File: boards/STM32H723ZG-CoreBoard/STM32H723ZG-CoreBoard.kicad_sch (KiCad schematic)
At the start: 44 parts, among them J1 USB-C, J2 PORT_L, J3 PORT_B, J4 PORT_R, J5 PORT_T, J6 SWD, SW1 RESET, SW2 BOOT0, U1 STM32H723ZGT6, U2 AP2112K-3.3, Y1 25MHz, Y2 32.768kHz

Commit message: Довести H723 до KiCad 10: разъём прошивки, STDC14, переразметка верхнего кольца
Плата H723 пересобрана в формате KiCad 10 и подтянута к раскладке G474.

Плата:
- разъём прошивки J6 - 1x10 с распиновкой WeAct, развёрнут 5V к востоку,
  SWO садится на PB3 прямой дорожкой;
- добавлен J7 - STDC14 (2x7, 1.27 мм), штатный разъём ST-LINK V3. Стоит
  вертикально сигнальным рядом к J6: строки веера идут по строкам падов и
  между собой не пересекаются, а расходятся по слоям;
- USB-C стоит на плате целиком, D+/D- заведены на PA11/PA12;
- кнопки RST и BOOT0 собраны в колонку у левого края, R4 - вплотную к SW2;
- светодиод и резистор развёрнуты под 45 градусов в углу между J2 и J3;
- подписаны все 144 контакта гребёнок и номиналы всех компонентов.

Генератор:
- gen/kicadenv.py - поиск библиотек KiCad на любой ОС и различия API 7/10;
- gen/export.py - гербера, сверловка, pos.csv, PDF и архив через kicad-cli;
- сборка платы больше не зависит от системных библиотек: футпринты уходят в
  auto_probe.pretty рядом с платой;
- kigen.py: разбор многострочной формы pin_names/pin_numbers KiCad 10 -
  из-за неё поверх номеров контактов печатались имена;
- crtyd.py считает пересечение реальных полигонов, а не описанных
  прямоугольников; drc.py не считает нарушением зазор ровно по правилу.

Проверки H723: DRC KiCad 0 нарушений, 0 несоединённых, 0 расхождений со
схемой; собственный контроль зазоров 0, courtyard 0, шелкография 0.
Файлы платы G474 не тронуты, правки в build_g474.py - только переносимость.

Co-Authored-By: Claude Opus 5 <noreply@anthropic.com>
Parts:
- removed J6: SWD, Connector_PinHeader_2.54mm:PinHeader_1x04_P2.54mm_Vertical, symbol Connector_Generic:Conn_01x04
- added J6: DEBUG, auto_probe:PinHeader_1x10_P2.54mm_Vertical, symbol Connector_Generic:Conn_01x10
- added J7: STDC14, auto_probe:PinHeader_2x07_P1.27mm_Vertical, symbol Connector_Generic:Conn_02x07_Odd_Even
- C1, C10, C11, C2, C3, C4, C5, C6, C60, C61, C62, C63, C7, C70, C74, C77, C8, C9: footprint :C_0402_1005Metric -> auto_probe:C_0402_1005Metric
- C50, C51, C75, C76: footprint :C_0805_2012Metric -> auto_probe:C_0805_2012Metric
- C52, C71, C72, C73: footprint :C_0603_1608Metric -> auto_probe:C_0603_1608Metric
- D1: footprint LED_SMD:LED_0805_2012Metric -> auto_probe:LED_0805_2012Metric
- J1: footprint Connector_USB:USB_C_Receptacle_HRO_TYPE-C-31-M-12 -> auto_probe:USB_C_Receptacle_HRO_TYPE-C-31-M-12
- J2, J3, J4, J5: footprint Connector_PinHeader_2.54mm:PinHeader_2x18_P2.54mm_Vertical -> auto_probe:PinHeader_2x18_P2.54mm_Vertical
- R1, R2, R3, R4, R5: footprint Resistor_SMD:R_0402_1005Metric -> auto_probe:R_0402_1005Metric
- SW1, SW2: footprint Button_Switch_SMD:SW_SPST_SKQG_WithoutStem -> auto_probe:SW_SPST_SKQG_WithoutStem
- U1: footprint Package_QFP:LQFP-144_20x20mm_P0.5mm -> auto_probe:LQFP-144_20x20mm_P0.5mm
- U2: footprint Package_TO_SOT_SMD:SOT-23-5 -> auto_probe:SOT-23-5
- Y1: footprint Crystal:Crystal_SMD_5032-2Pin_5.0x3.2mm -> auto_probe:Crystal_SMD_5032-2Pin_5.0x3.2mm
- Y2: footprint Crystal:Crystal_SMD_MicroCrystal_CC7V-T1A-2Pin_3.2x1.5mm -> auto_probe:Crystal_SMD_MicroCrystal_CC7V-T1A-2Pin_3.2x1.5mm
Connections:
- net +3V3: now also J6.10 (Pin_10), J7.3 (Pin_3)
- net GND: now also J1.SH (SHIELD), J6.2 (Pin_2), J6.7 (Pin_7), J7.11 (Pin_11), J7.5 (Pin_5), J7.7 (Pin_7); no longer J1.S1 (SHIELD)
- net NRST: now also J6.5 (Pin_5), J7.12 (Pin_12)
- net PB3: now also J6.6 (Pin_6), J7.8 (Pin_8)
- net PC10: now also J6.3 (Pin_3)
- net PC11: now also J6.4 (Pin_4)
- net SWCLK: now also J6.8 (Pin_8), J7.6 (Pin_6)
- net SWDIO: now also J6.9 (Pin_9), J7.4 (Pin_4)
- net VBUS: now also J6.1 (Pin_1)
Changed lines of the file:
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@@
 (kicad_sch (version 20230121) (generator kigen)
-  (paper "A2")
+  (paper "A1")
   (title_block
     (title "STM32H723ZGT6 core board (LQFP144) - 84x84 mm, 4 layers")

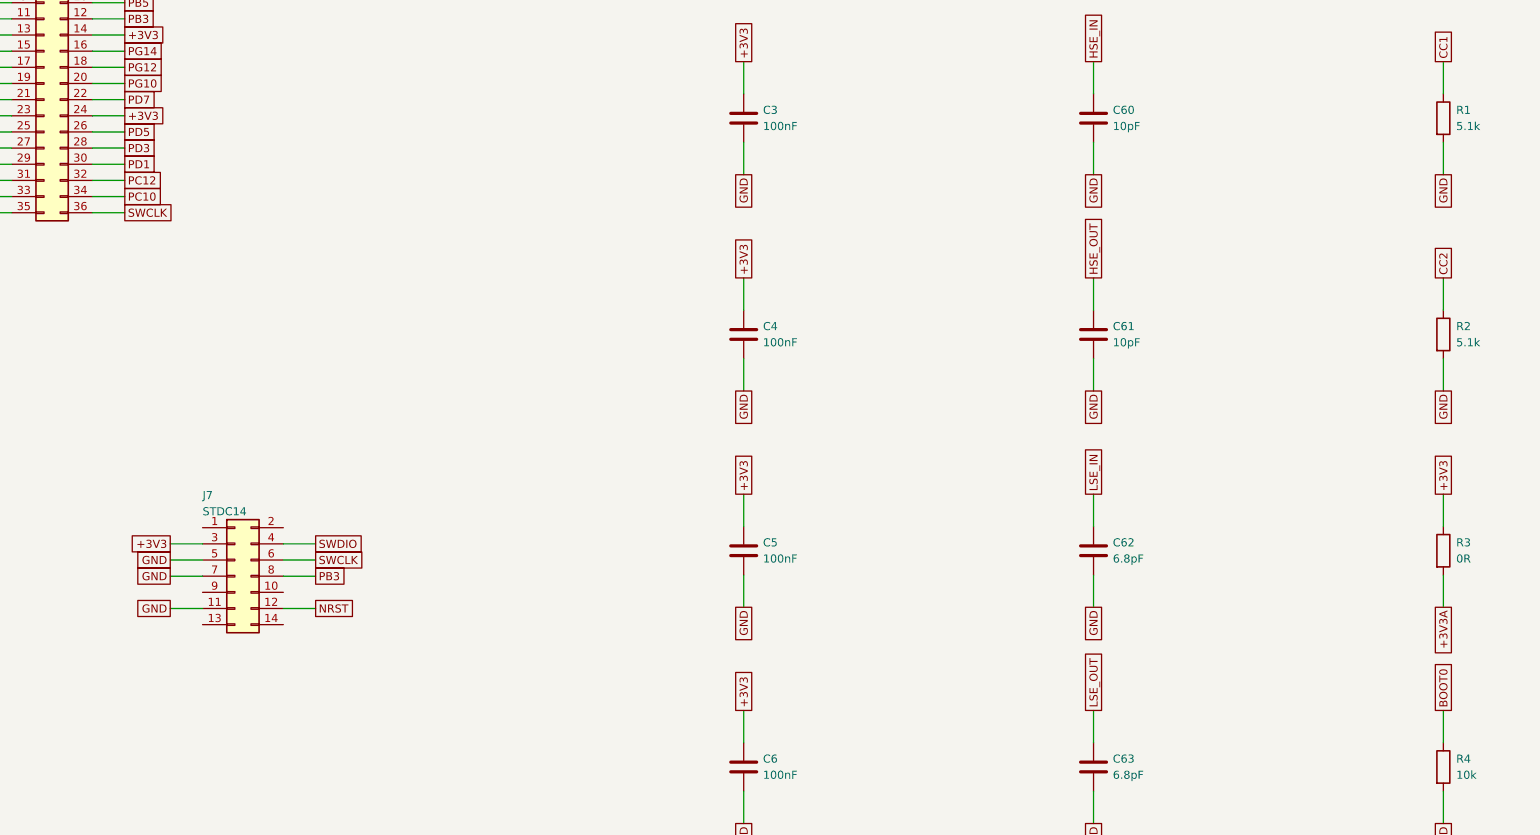
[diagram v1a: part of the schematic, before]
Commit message: H723: убрать STDC14, переразметить верхнее кольцо и шелкографию под нормы печати
Разъём прошивки и его окружение:
- STDC14 (J7) снят с платы, из схемы и из библиотеки проекта: вертикально он
  занимал 7.6 мм по высоте и не давал поднять J6;
- J6 поднят к верхнему краю (Y0+5.2), обозначение закреплено в торце справа;
- полосы SWO/CLK/DIO отведены от контура: было 0.67 мм до фрезы, стало 1.67;
- BOOT0 к гребёнке обходит J6 западнее, отвод +3V3 от контакта 10 смотрит вверх.

Шелкография приведена к нормам JLCPCB (0.8 мм при линии 0.15):
- подписи контактов были 0.6/0.1, номиналы на обратной стороне 0.5 - мельче
  минимума, при печати такие символы плывут;
- строки подписей отодвинуты от гребёнок, внешние выставлены по центру кольца:
  крупный шрифт задевал контур разъёма и свешивался за край платы;
- в кольце 3.7 мм, пятизначное имя туда не входит - для нескольких цепей на
  шелке короткая форма (3V3A, PC2C, USBDP); в схеме и PINOUT.csv имена полные;
- у деталей печатается только обозначение, номиналы собраны в таблицу
  "обозначение - номинал" на 35 строк в двух свободных площадках у J4;
- обозначение ставится строго над своей деталью горизонтально: раньше список
  занятых мест включал их же штатные позиции, подпись конфликтовала сама с
  собой и уезжала в сторону под произвольным углом.

Расхождения со схемой (видны только в GUI, CLI их не показывает):
- висящим выводам проставлены те же имена, что генерирует eeschema
  (unconnected-(REF-ИМЯ-PadN)) - 9 штук;
- крепёжные отверстия добавлены в схему, с футпринта снята пометка "не в BOM";
- номинал R3 в схеме сведён с платой (0R/FB).

Развязка: C74 перенесён от края к своему выводу VDD33USB (было 25.5 мм, стало
5.9), места в сетке под корпусом раздаются по близости к своему выводу
(в среднем 12.4 -> 9.4 мм).

silkchk.py теперь ловит шелк за контуром платы - KiCad этого не проверяет.

Проверки H723: DRC KiCad 0 нарушений и 0 предупреждений, 0 несоединённых,
0 расхождений со схемой; свой контроль зазоров 0, courtyard 0, ш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
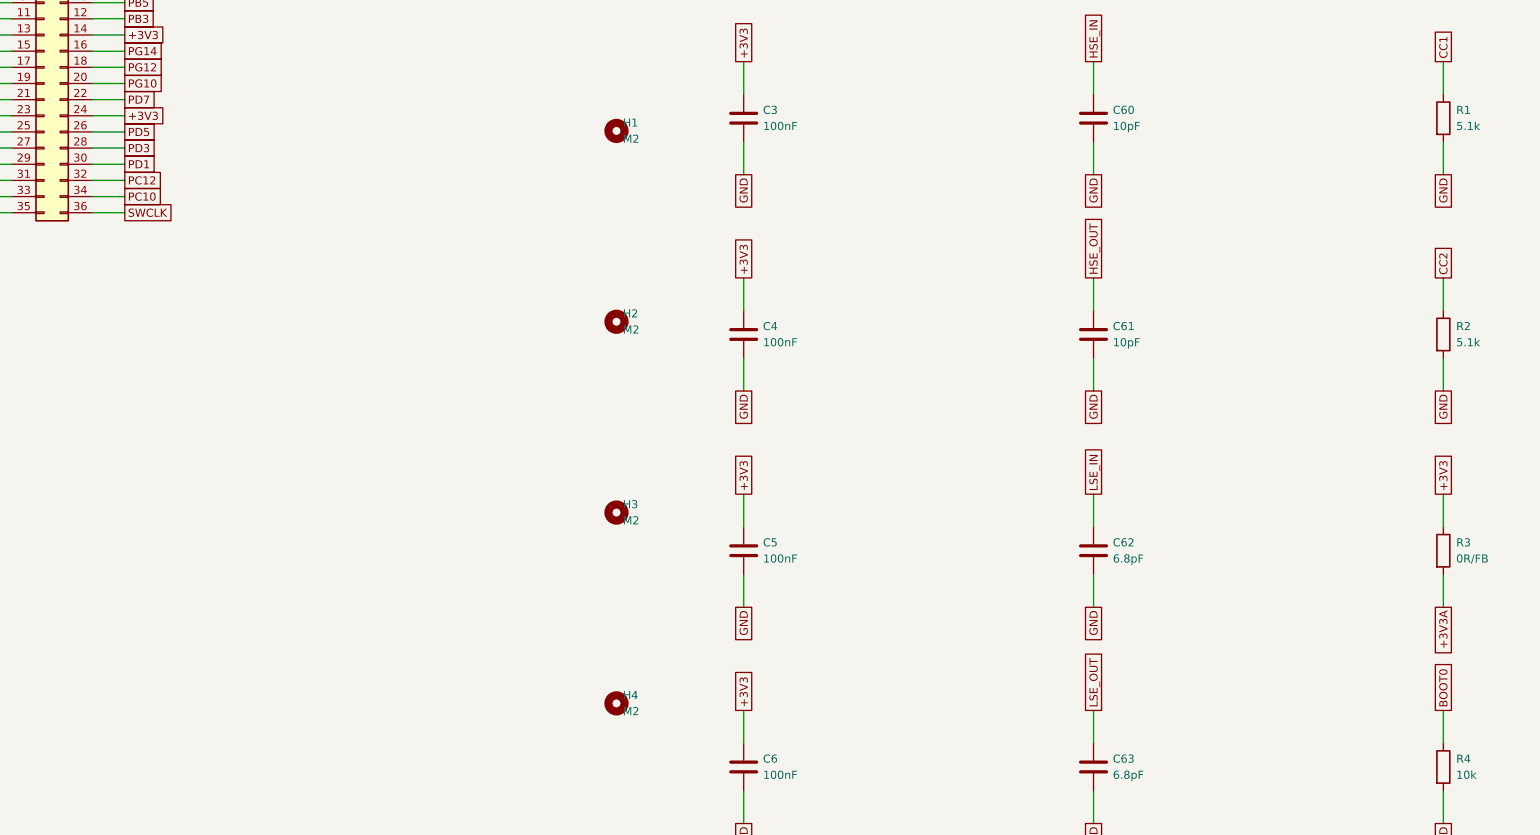
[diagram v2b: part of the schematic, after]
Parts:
- removed J7: STDC14, auto_probe:PinHeader_2x07_P1.27mm_Vertical, symbol Connector_Generic:Conn_02x07_Odd_Even
- added H1, H2, H3, H4: M2, auto_probe:MountingHole_2.2mm_M2, symbol Mechanical:MountingHole
- R3: value 0R -> 0R/FB

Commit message: H723: кварц под наличие JLCPCB, номера LCSC в BOM, выходные файлы в их формате
Кварц HSE переведён на корпус, который у JLCPCB есть как Basic Part:
- Y1 - SMD-3225 с четырьмя падами (Yangxing X322525MOB4SI, C9006) вместо
  двухпадового 5032: тот только Extended и с перебоями в наличии;
- сигнальные пады у 3225 стоят по диагонали, между ними земляные, поэтому оба
  сигнала заходят с запада разными колонками, а отвод HSE_OUT к своей банке
  идёт под корпусом;
- экранные пады связаны диагональю под кварцем и посажены на полигон одной via:
  вокруг проходит веер J2, второй via там не встаёт;
- нагрузочная ёмкость нового кварца 12 пФ, поэтому обвязка обоих генераторов
  пересчитана с 10 и 6.8 пФ на 18 пФ (C60-C63).

Выходные файлы приведены к формату JLCPCB:
- pos.csv переименовывает колонки в Designator / Mid X / Mid Y / Rotation /
  Layer - родные заголовки KiCad их парсер отвергает целиком;
- BOM.csv собран из Comment / Designator / Footprint / LCSC Part #;
- крепёжные отверстия из сборочного BOM убраны: все пады неметаллизированные,
  паять нечего, а JLCPCB ругался на их отсутствие в CPL;
- проставлены номера LCSC на 22 позиции из списка Basic Parts, для кварцев
  вместо номера - требование по нагрузочной ёмкости, для AP2112K - замена по
  выводам ME6211C33M5G-N (C82942) на случай дефицита.

Шелкография: у D1 подписана полярность (+/- сбоку от падов, по цепям LED_A и
LED_K), обозначения деталей ставятся строго над корпусом горизонтально.

Проверки H723: DRC KiCad 0 нарушений и 0 предупреждений, 0 несоединённых,
0 расхождений со схемой; свой контроль зазоров 0, courtyard 0, шелкография
0 наложений, 0 поверх падов, 0 за контуром.

Co-Authored-By: Claude Opus 5 <noreply@anthropic.com>
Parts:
- removed Y1: 25MHz, auto_probe:Crystal_SMD_5032-2Pin_5.0x3.2mm, symbol Device:Crystal
- added Y1: 25MHz, auto_probe:Crystal_SMD_3225-4Pin_3.2x2.5mm, symbol Device:Crystal_GND24
- C60, C61: value 10pF -> 18pF
- C62, C63: value 6.8pF -> 18pF
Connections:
- net GND: now also Y1.2 (G), Y1.4 (G)
- net HSE_IN: now also Y1.1
- net HSE_OUT: now also Y1.3
